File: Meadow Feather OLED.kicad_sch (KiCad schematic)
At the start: 15 parts, among them J1 Meadow_F7_Feather, J2 Conn_01x04

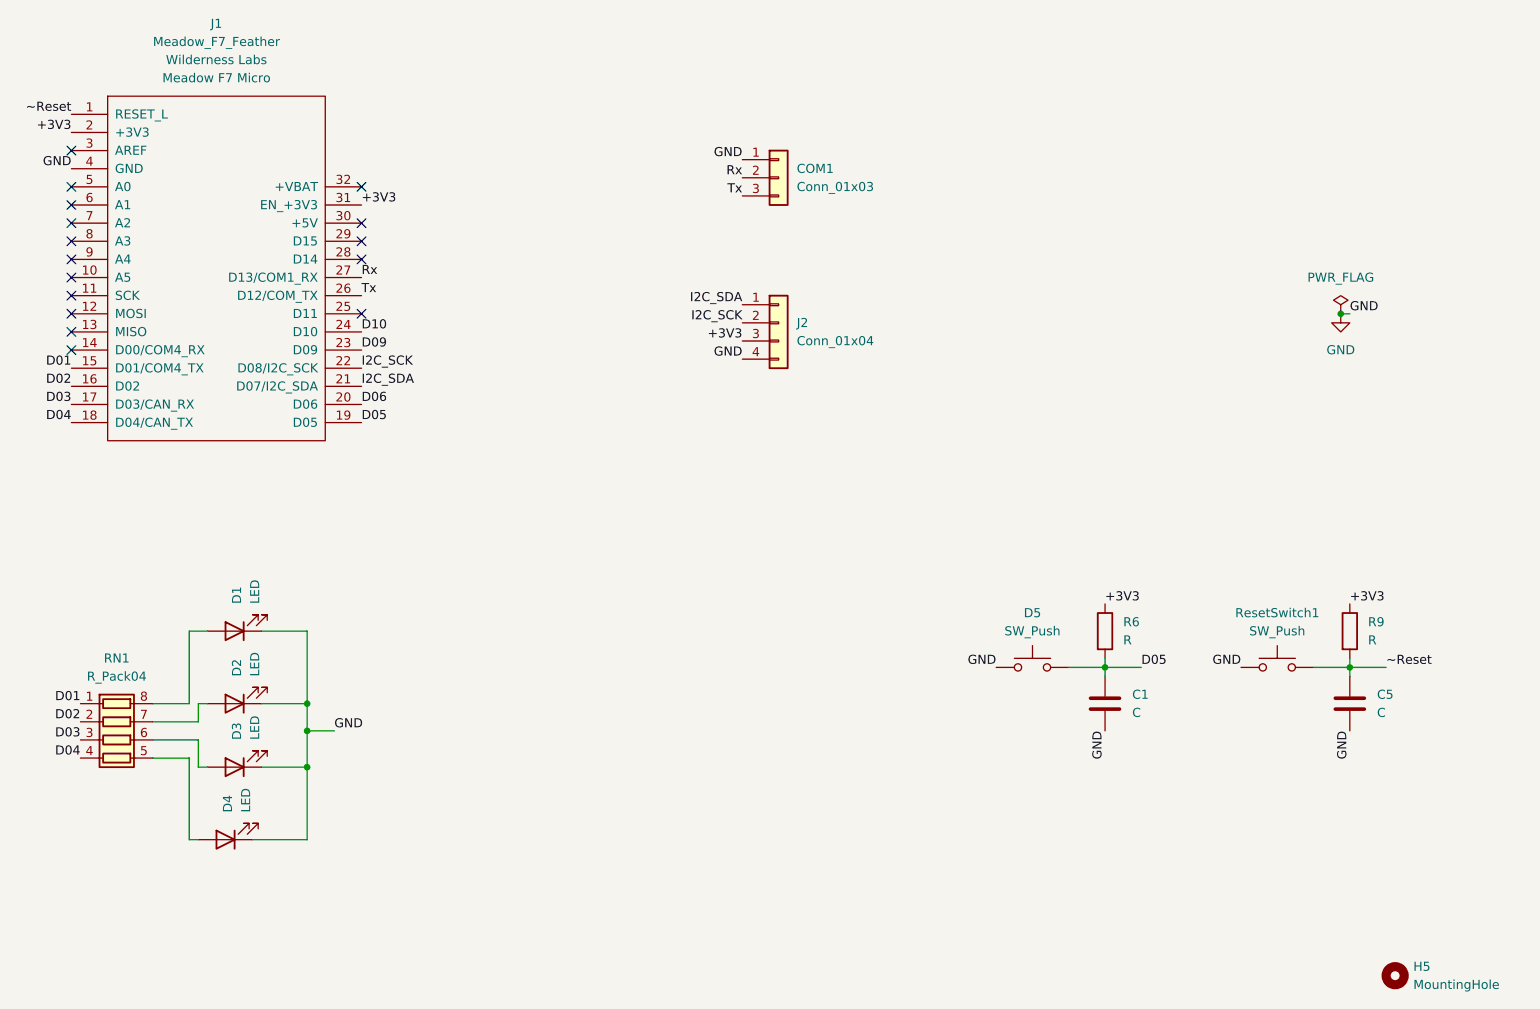
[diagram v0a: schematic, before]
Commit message: Updated to V2.1 fixing: * Unconnected D3 and GND * Rounded tracks for the 1970s feel * Corrected LED resistor footprint
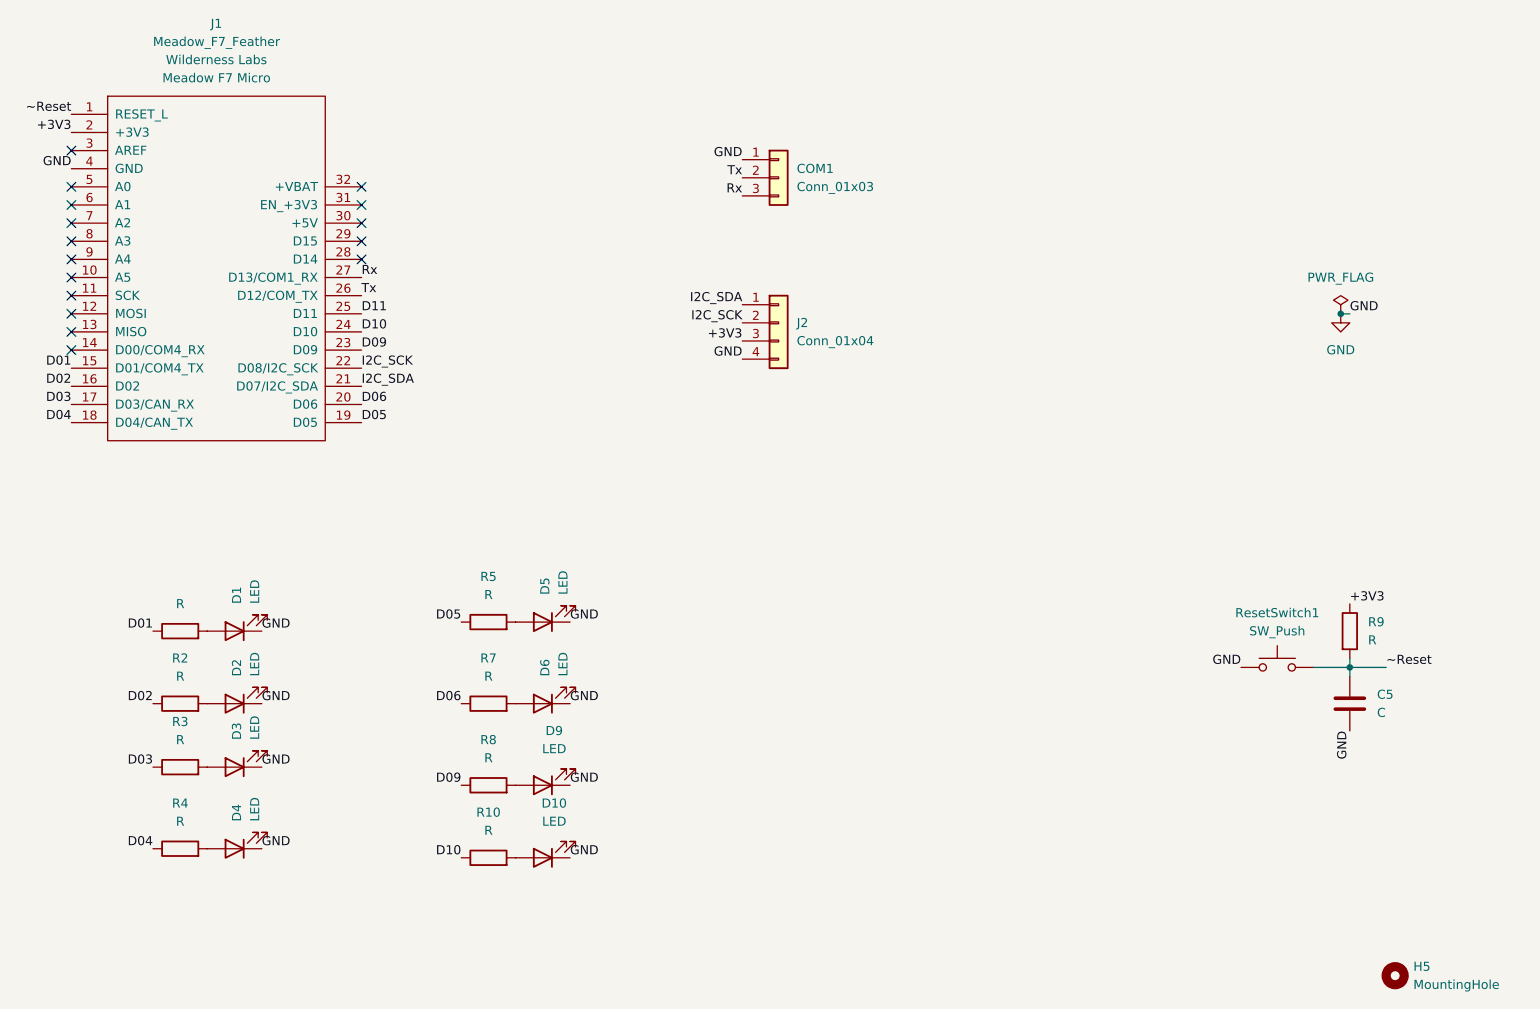
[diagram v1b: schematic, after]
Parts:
- removed C1: C, Capacitor_SMD:C_0603_1608Metric_Pad1.08x0.95mm_HandSolder, symbol Device:C
- removed D5: SW_Push, Connector_PinHeader_2.54mm:PinHeader_1x03_P2.54mm_Vertical, symbol Switch:SW_Push
- removed R6: R, Resistor_SMD:R_0805_2012Metric_Pad1.20x1.40mm_HandSolder, symbol Device:R
- removed RN1: R_Pack04, Resistor_SMD:R_Array_Convex_4x1206, symbol Device:R_Pack04
- added D10, D5, D6, D9: LED, LED_SMD:LED_0603_1608Metric_Pad1.05x0.95mm_HandSolder, symbol Device:LED
- added R1, R10, R2, R3, R4, R5, R7, R8: R, Resistor_SMD:R_0603_1608Metric_Pad0.98x0.95mm_HandSolder, symbol Device:R
- J1: footprint MCU_Wilderness_Labs:MeadowF7MicroFeatherOutline -> MCU_WildernessLabs:MeadowF7MicroFeatherOutline
- R9: footprint Resistor_SMD:R_0805_2012Metric_Pad1.20x1.40mm_HandSolder -> Resistor_SMD:R_0603_1608Metric_Pad0.98x0.95mm_HandSolder
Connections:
- net +3V3: no longer J1.31 (EN_+3V3)
- net D01: now also R1.1
- net D02: now also R2.1
- net D03: now also R3.1
- net D04: now also R4.1
- net D05: now also R5.1
- net D06: now also R7.1
- net D09: now also R8.1
- net D10: now also R10.1
- net GND: now also D10.1 (K), D5.1 (K), D6.1 (K), D9.1 (K)
- net Rx: now also COM1.3 (Pin_3); no longer COM1.2 (Pin_2)
- net Tx: now also COM1.2 (Pin_2); no longer COM1.3 (Pin_3)
- net D11: now reaches J1.25 (D11)
- net at D2.2 (A): now also R2.2
- net at D4.2 (A): now also R4.2
- net at D1.2 (A): now also R1.2
- net at D3.2 (A): now also R3.2
- new net: D9.2 (A), R8.2
- new net: D6.2 (A), R7.2
- new net: D5.2 (A), R5.2
- new net: D10.2 (A), R10.2
